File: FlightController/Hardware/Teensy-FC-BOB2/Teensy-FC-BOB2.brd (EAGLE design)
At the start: 100 x 80 mm, 37 parts, among them U1 MPU-9250, U3 BMP180;314030004

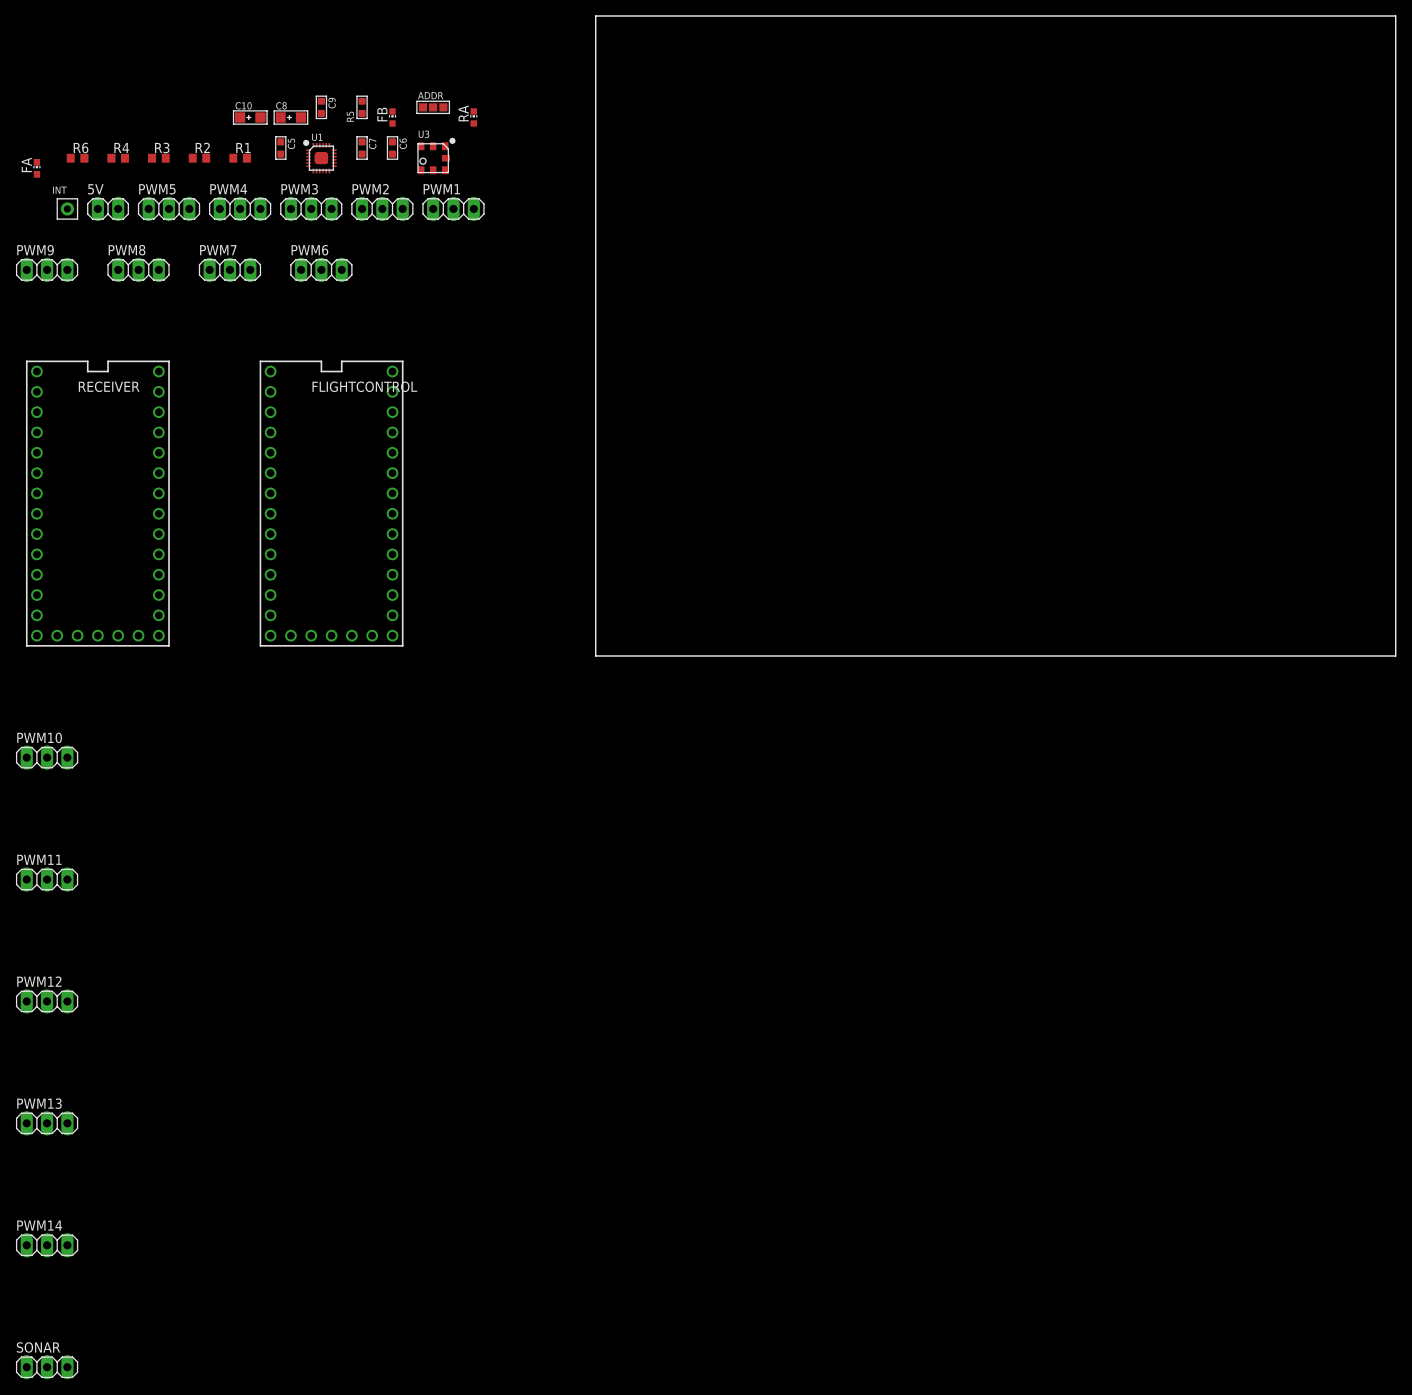
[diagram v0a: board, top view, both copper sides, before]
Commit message: autoroutes the pub
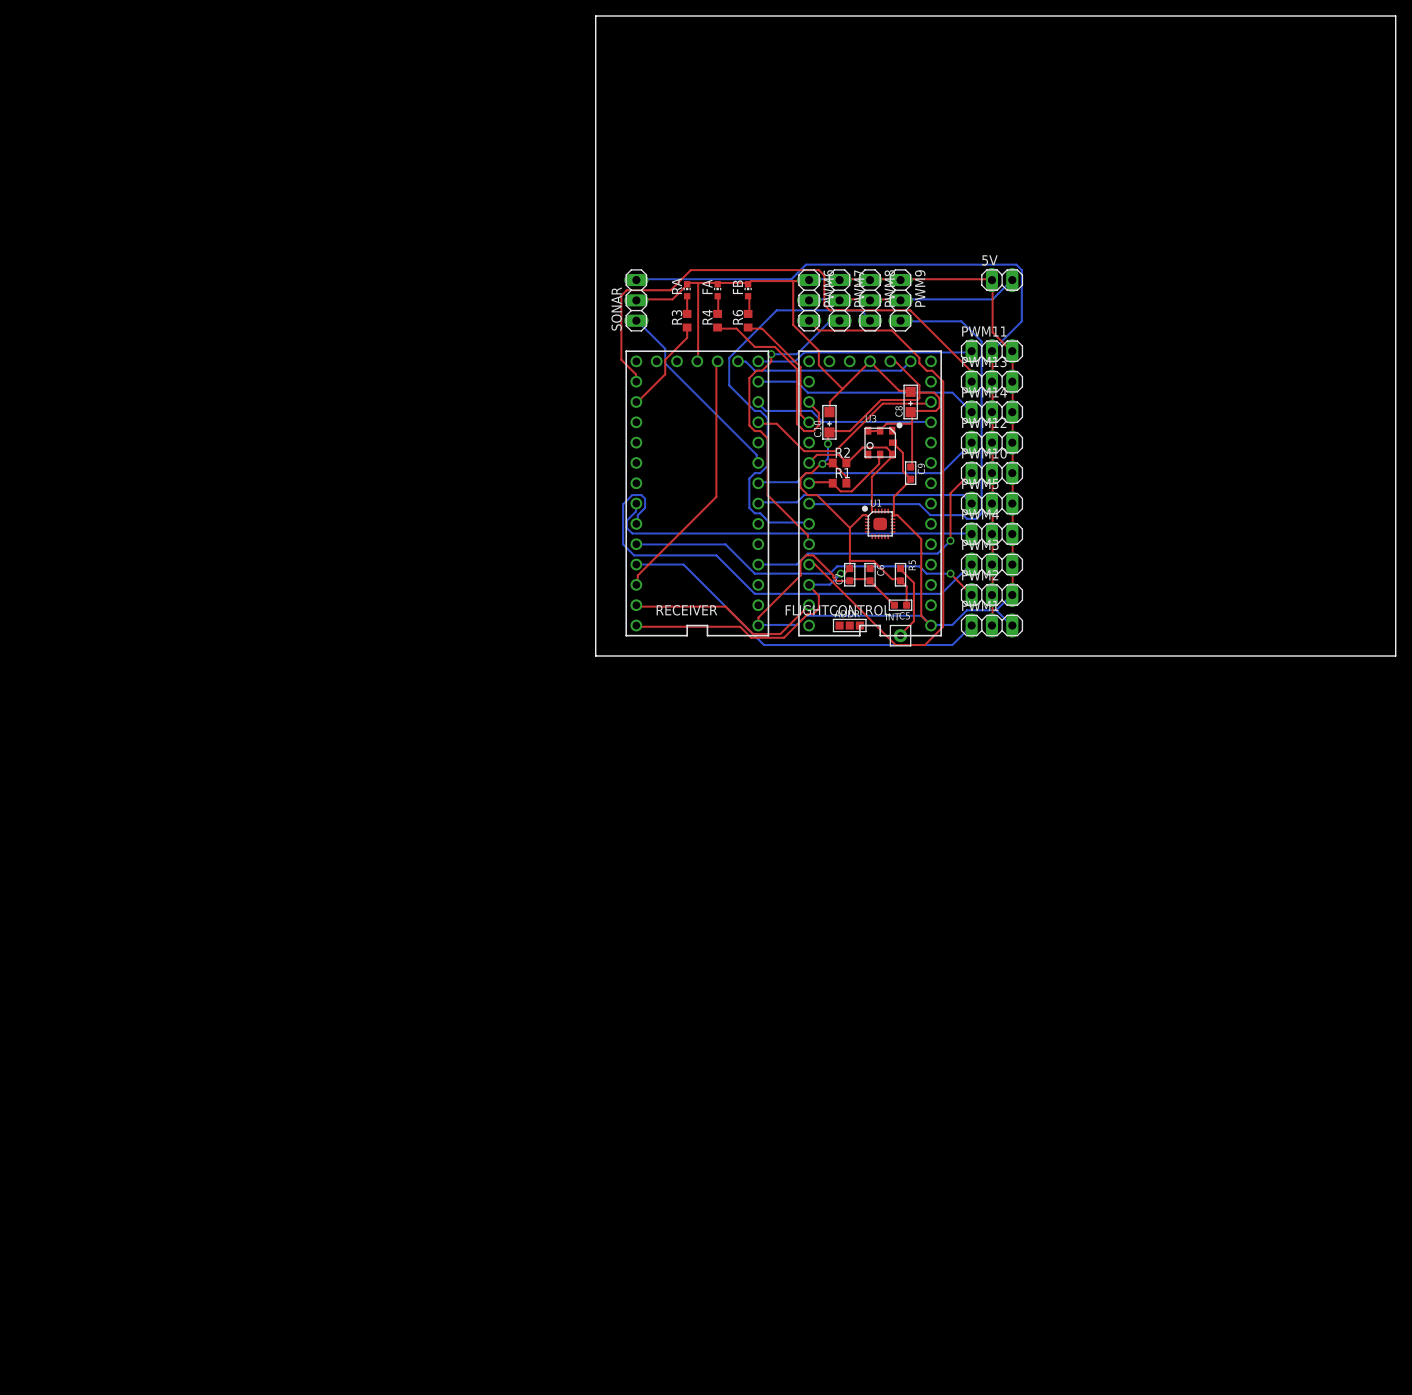
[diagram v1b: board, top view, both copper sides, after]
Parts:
- moved PWM14 157.5 mm to (49.5, 30.5)
- moved SONAR 152.3 mm to (5.08, 44.5), turned to 90 degrees
- moved PWM13 150.2 mm to (49.5, 34.3)
- moved PWM12 137.2 mm to (49.5, 26.7)
- moved PWM11 135.3 mm to (49.5, 38.1)
- moved PWM10 123.3 mm to (49.5, 22.9)
- moved INT 117.0 mm to (38.1, 2.54)
- moved 5V 112.1 mm to (50.8, 47.0)
- moved PWM5 109.3 mm to (49.5, 19.1)
- moved PWM9 106.7 mm to (38.1, 44.5), turned to 270 degrees
- moved PWM4 102.4 mm to (49.5, 15.2)
- moved C5 96.3 mm to (38.1, 6.35), turned to 270 degrees
- moved PWM3 96.0 mm to (49.5, 11.4)
- moved PWM8 91.5 mm to (34.3, 44.5), turned to 270 degrees
- moved PWM2 90.2 mm to (49.5, 7.62)
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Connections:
- new net N$20: PWM10.1, RECEIVER.2
- new net N$23: PWM12.1, RECEIVER.6
- new net N$24: PWM14.1, RECEIVER.11
- new net N$25: PWM11.1, RECEIVER.12
- new net N$26: PWM13.1, RECEIVER.14/A0
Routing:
- net GND: track 0.00 -> 217.5 mm
- net VCC_3V3: track 0.00 -> 115.2 mm, vias 0 -> 3
- net N$22: track 0.00 -> 95.7 mm
- net N$13: track 0.00 -> 72.8 mm
- net N$26: track 0.00 -> 65.4 mm
- net N$7: track 0.00 -> 59.7 mm
- net N$10: track 0.00 -> 55.3 mm
- net N$11: track 0.00 -> 51.5 mm
- net N$5: track 0.00 -> 47.1 mm
- net N$8: track 0.00 -> 46.9 mm
- net N$6: track 0.00 -> 45.3 mm, vias 0 -> 1
- net N$12: track 0.00 -> 39.0 mm, vias 0 -> 1
- net N$20: track 0.00 -> 34.9 mm, vias 0 -> 1
- net 3.3V: track 0.00 -> 32.3 mm
- net N$23: track 0.00 -> 28.8 mm
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
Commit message: final pcb
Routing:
- net VCC_3V3: track 115.2 -> 150.5 mm, vias 3 -> 8
- net GND: track 217.5 -> 238.1 mm, vias 0 -> 2
- net AD0/SDO: track 0.00 -> 14.8 mm, vias 0 -> 4
- net SCL/SCLK: track 12.0 -> 18.6 mm, vias 0 -> 2
- net N$4: track 9.74 -> 16.3 mm, vias 0 -> 2
- net N$3: track 0.00 -> 4.60 mm
- net N$6: track 45.3 -> 46.6 mm
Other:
- board size 100 x 80 mm -> 61.4 x 55.1 mm

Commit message: add
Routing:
- net GND: track 238.1 -> 237.4 mm
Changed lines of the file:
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@@
 <setting verticaltext="up"/>
 </settings>
-<grid distance="1" unitdist="mm" unit="mm" style="lines" multiple="1" display="no" altdistance="0.025" altunitdist="inch" altunit="inch"/>
+<grid distance="0.1" unitdist="mm" unit="mm" style="lines" multiple="1" display="no" altdistance="0.025" altunitdist="inch" altunit="inch"/>
 <layers>
 <layer number="1" name="Top" color="4" fill="1" visible="yes" active="yes"/>
@@
 <wire x1="52.1208" y1="22.86" x2="52.07" y2="22.86" width="0.254" layer="1"/>
 <wire x1="37.719" y1="17.6022" x2="37.2618" y2="17.6022" width="0.254" layer="1"/>
-<wire x1="40.1447" y1="17.1323" x2="40.259" y2="14.6304" width="0.254" layer="1"/>
-<wire x1="40.1447" y1="17.1323" x2="37.719" y2="17.6022" width="0.254" layer="1"/>
+<wire x1="40.252084375" y1="15.404928125" x2="40.259" y2="14.6304" width="0.254" layer="1"/>
+<wire x1="40.252084375" y1="15.404928125" x2="40.2447" y2="16.2323" width="0.254" layer="1"/>
 <wire x1="40.259" y1="5.0292" x2="40.259" y2="14.6304" width="0.254" layer="1"/>
 <wire x1="41.91" y1="3.81" x2="40.259" y2="5.0292" width="0.254" layer="1"/>
@@
 <wire x1="37.1602" y1="19.7866" x2="37.2618" y2="19.8882" width="0.254" layer="1"/>
 <wire x1="36.1696" y1="18.11" x2="36.1696" y2="19.4056" width="0.254" layer="1"/>
-<wire x1="38.2016" y1="14.6558" x2="40.1447" y2="17.1323" width="0.254" layer="1"/>
 <wire x1="33.02" y1="3.81" x2="33.02" y2="3.4036" width="0.254" layer="1"/>
 <wire x1="33.02" y1="3.4036" x2="34.1122" y2="2.3114" width="0.254" layer="1"/>
@@
 <wire x1="36.16" y1="14.91" x2="36.16" y2="12.5826" width="0.254" layer="1"/>
 <wire x1="37.1602" y1="12.2682" x2="38.2016" y2="13.3604" width="0.254" layer="1"/>
-<wire x1="38.2016" y1="13.3604" x2="38.2016" y2="14.6558" width="0.254" layer="1"/>
 <wire x1="36.4744" y1="12.2682" x2="37.1602" y2="12.2682" width="0.254" layer="1"/>
+<wire x1="40.2447" y1="16.2323" x2="40.2447" y2="16.6553" width="0.254" layer="1"/>
+<wire x1="40.2447" y1="16.6553" x2="39.3" y2="17.6" width="0.254" layer="1"/>
+<wire x1="39.3" y1="17.6" x2="37.7212" y2="17.6" width="0.254" layer="1"/>
+<wire x1="37.7212" y1="17.6" x2="37.719" y2="17.6022" width="0.254" layer="1"/>
+<wire x1="38.2016" y1="14.9016" x2="38.6" y2="15.3" width="0.254" layer="1"/>
+<wire x1="38.6" y1="15.3" x2="40.14715625" y2="15.3" width="0.254" layer="1"/>
+<wire x1="40.14715625" y1="15.3" x2="40.252084375" y2="15.404928125" width="0.254" layer="1"/>
+<wire x1="38.2016" y1="13.3604" x2="38.2016" y2="14.9016" width="0.254" layer="1"/>
 </signal>
 <signal name="VCC_3V3">
